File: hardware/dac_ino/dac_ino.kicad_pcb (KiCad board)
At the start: 2 copper layers, 94 x 91 mm, 84 parts, among them J1 Conn_01x03_Male, J10 Conn_01x04, J11 Conn_01x02, J12 Molex 2 pin GATE IN, J13 Molex 2 pin GATE IN, J14 Conn_01x01_Units, J15 Molex 2 pin CV IN, J16 Molex 2 pin CV IN, J17 Molex 2 pin CV IN, J18 Molex 2 pin CV IN, J19 Molex 2 pin GATE IN, J2 Conn_01x03_Male, J20 Molex 2 pin GATE IN, J21 Conn_01x06, J3 Molex 2 pin CV OUT, J4 Molex 2 pin CV OUT, J5 Molex 2 pin GATE OUT, J6 Molex 2 pin GATE OUT, J7 Conn_01x01_Units, J8 Molex 2 pin VCC, J9 EURO_PWR_2x5, Q1 2N3904, Q2 2N3904, Q3 2N3904, Q4 2N3904, Q5 2N3904, Q6 2N3904, U1 MCP4922, U2 TL072, U3 REF02CP+

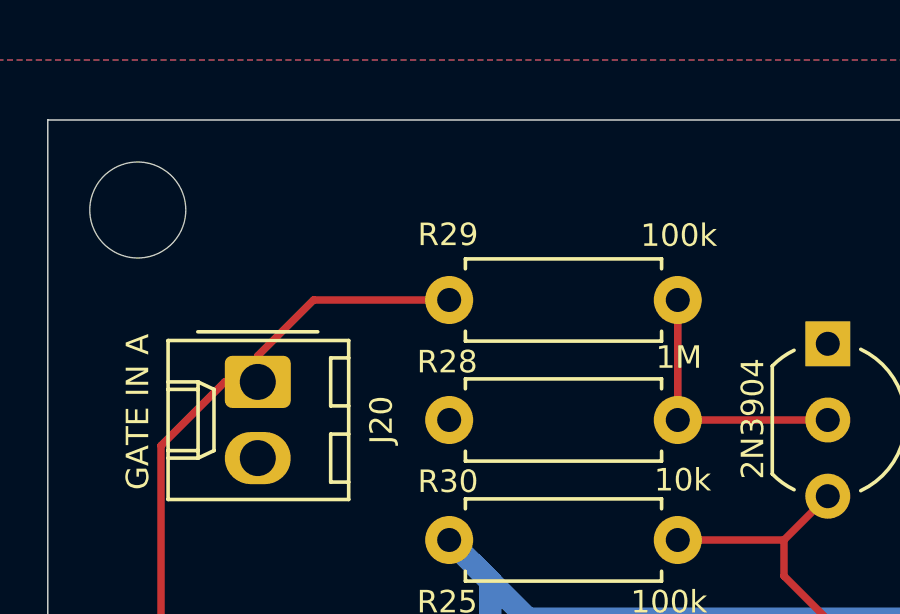
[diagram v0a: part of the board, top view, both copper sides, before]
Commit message: Fix silkscreen error
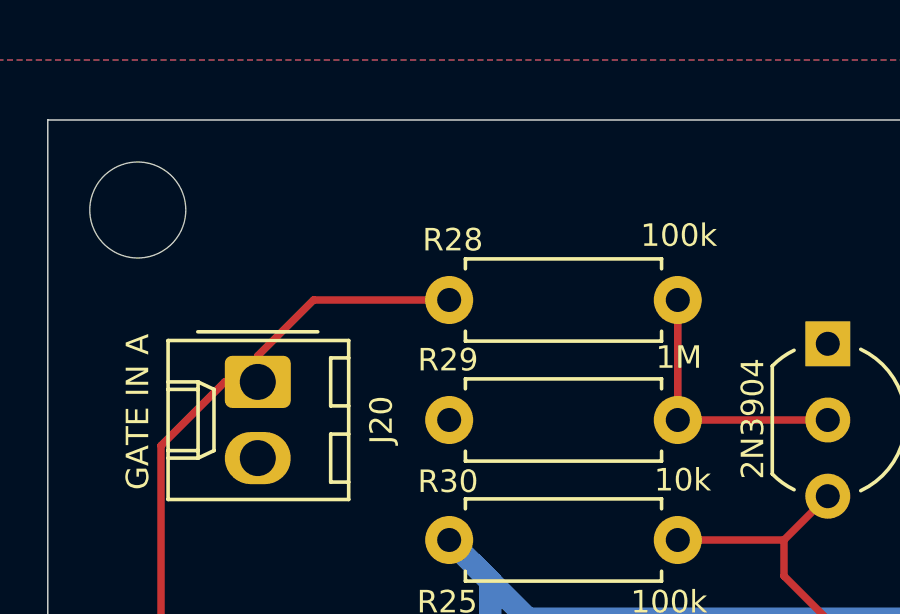
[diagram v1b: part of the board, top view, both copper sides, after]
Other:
- board text added: "dac/ino v. 1.31 • Rich Holmes 7/2020 • from Synapse by Vincenzo Pacella • cc-by-ca"
- board text removed: "dac/ino • Rich Holmes 7/2020 • from Synapse by Vincenzo Pacella • cc-by-ca"
